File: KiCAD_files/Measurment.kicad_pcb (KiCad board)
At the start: 2 copper layers, 90 x 63 mm, 66 parts, among them J1 Board outline, J2 Measurment_stage_outline_sign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, J3 Conn_01x02, U1 NMA1505SC, U2 AMC1100, U3 AMC1100, U4 AMC1311, U5 R-78C5.0-1.0, U6 AMS1117-3.3, U7 NMA1505SC

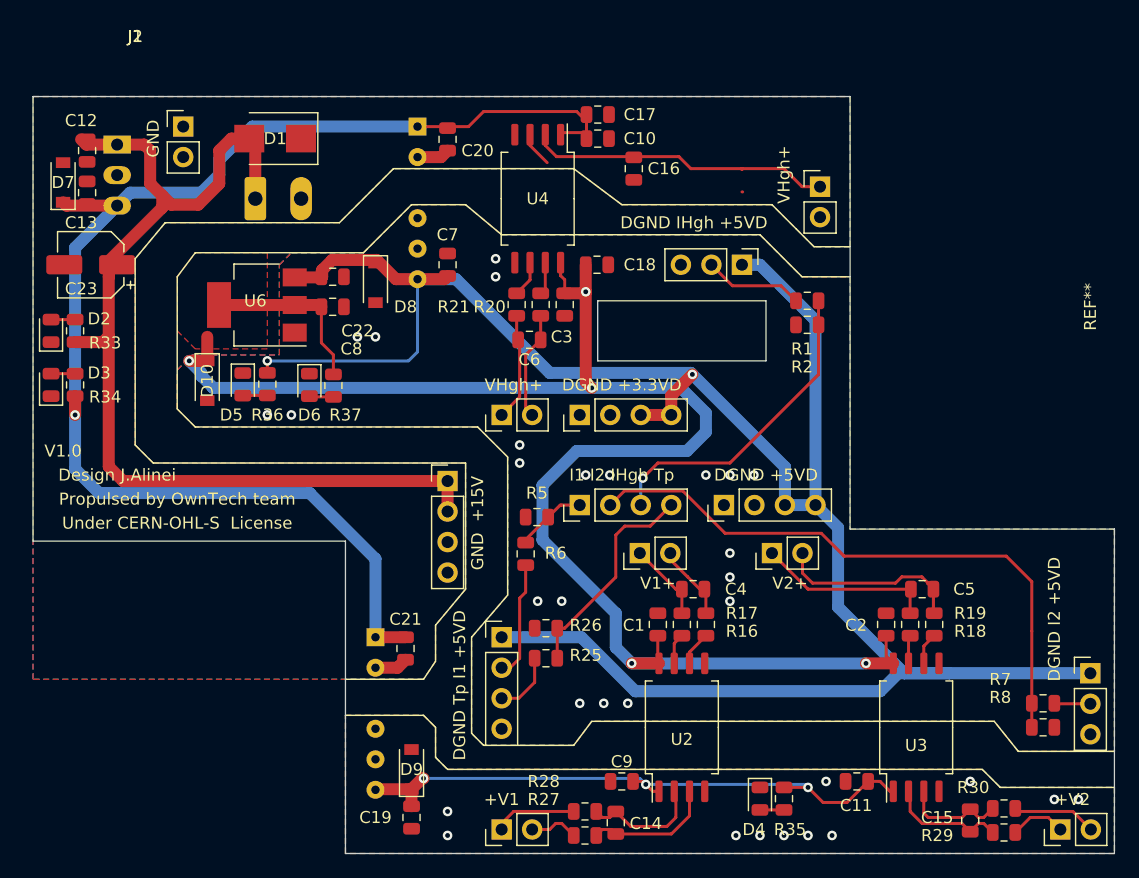
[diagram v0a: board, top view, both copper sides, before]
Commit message: Solved minor glitch on the overlay.
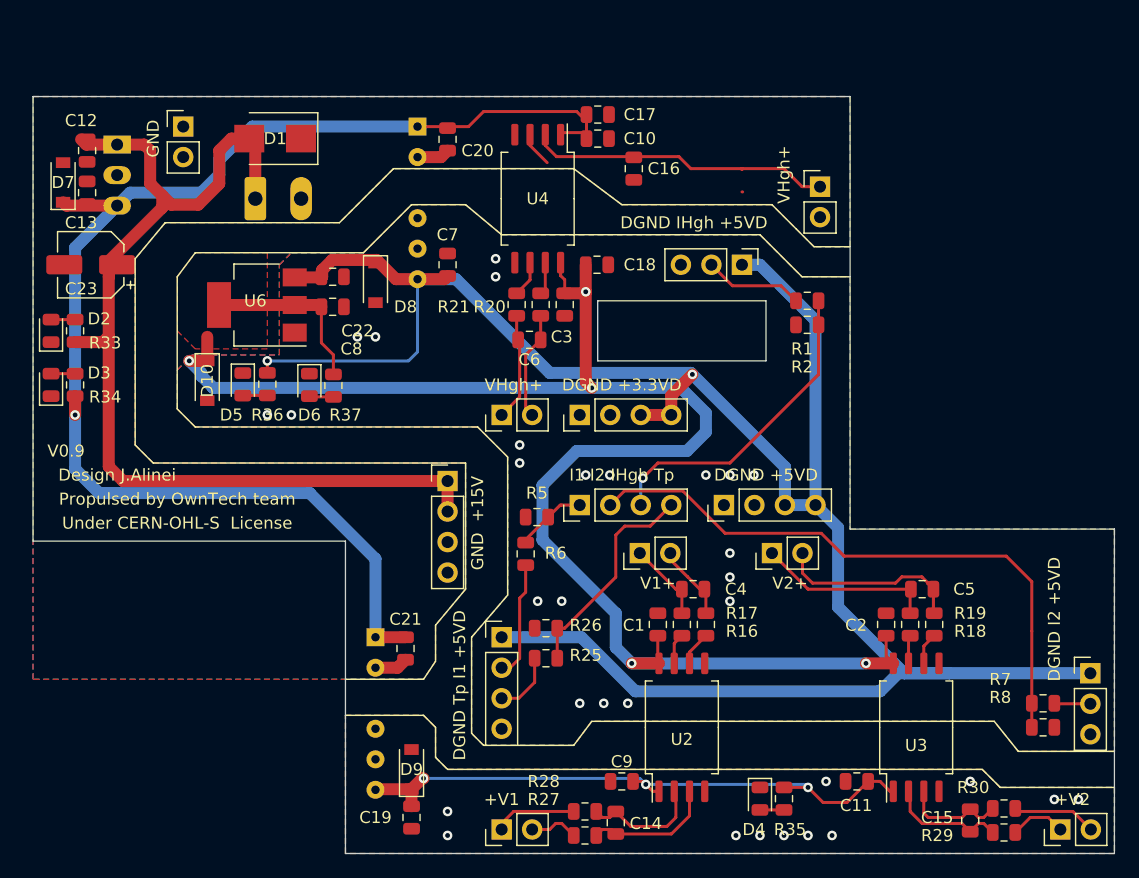
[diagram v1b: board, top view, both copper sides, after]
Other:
- board text added: "V0.9"
- board text removed: "V1.0"
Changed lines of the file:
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@@
   (general
     (thickness 1.6)
-    (drawings 66)
+    (drawings 64)
     (tracks 341)
     (zones 0)
@@
   (page A4)
   (layers
-    (0 F.Cu signal hide)
+    (0 F.Cu signal)
     (31 B.Cu signal hide)
     (32 B.Adhes user hide)
@@
   (module Footprints:Measurment_stage_outline_outputs (layer F.Cu)
     (at 31.5 41.5)
-    (fp_text reference J1 (at 8.5 -5 180) (layer F.SilkS)
+    (fp_text reference J1 (at 8.5 -5 180) (layer F.SilkS) hide
       (effects (font (size 1 1) (thickness 0.15)))
     )
@@
   (module Footprints:Measurment_stage_outline_inputs (layer F.Cu)
     (at 31.5 41.5)
-    (fp_text reference J2 (at 8.5 -5 180) (layer F.SilkS)
+    (fp_text reference J2 (at 8.5 -5 180) (layer F.SilkS) hide
       (effects (font (size 1 1) (thickness 0.15)))
     )
@@
     (fp_line (start 26 42) (end 26 63) (layer Eco2.User) (width 0.12))
     (fp_line (start 26 63) (end 90 63) (layer Eco2.User) (width 0.12))
-    (fp_text user REF** (at 88 17.5 270) (layer F.SilkS)
+    (fp_text user REF** (at 88 17.5 270) (layer F.SilkS) hide
       (effects (font (size 1 1) (thickness 0.15)))
     )
@@
       (effects (font (size 1 1) (thickness 0.15)) (justify mirror))
     )
-    (fp_text value Conn_01x02 (at 1.5 -18.5) (layer B.Fab)
+    (fp_text value Conn_01x02 (at 1.5 -18.5) (layer B.Fab) hide
       (effects (font (size 1 1) (thickness 0.15)) (justify mirror))
     )
@@
       (effects (font (size 1 1) (thickness 0.15)) (justify mirror))
     )
-    (fp_text value NMA1505SC (at 0.5 8.5 180) (layer B.Fab)
+    (fp_text value NMA1505SC (at 0.5 8.5 180) (layer B.Fab) hide
       (effects (font (size 1 1) (thickness 0.15)) (justify mirror))
     )
@@
       (effects (font (size 1 1) (thickness 0.15)) (justify mirror))
     )
-    (fp_text value NMA1505SC (at 9 -37) (layer B.Fab)
+    (fp_text value NMA1505SC (at 9 -37) (layer B.Fab) hide
       (effects (font (size 1 1) (thickness 0.15)) (justify mirror))
     )
@@
       (effects (font (size 1 1) (thickness 0.15)) (justify mirror))
     )
-    (fp_text value R-78C5.0-1.0 (at 3 16.5) (layer B.Fab)
+    (fp_text value R-78C5.0-1.0 (at 3 16.5) (layer B.Fab) hide
       (effects (font (size 1 1) (thickness 0.15)) (justify mirror))
     )
@@
     (effects (font (size 1 1) (thickness 0.15)))
   )
-  (gr_text "V1.0\n" (at 34 71) (layer F.SilkS)
+  (gr_text V0.9 (at 34.25 71) (layer F.SilkS)
     (effects (font (size 1 1) (thickness 0.15)))
   )
@@
   )
   (gr_line (start 31.5 41.5) (end 99.5 41.5) (layer Edge.Cuts) (width 0.05))
-  (gr_line (start 31.5 41.5) (end 26.5 41.5) (layer Dwgs.User) (width 0.15))
-  (gr_line (start 31.5 41.5) (end 31.5 38) (layer Dwgs.User) (width 0.15))
   (gr_line (start 80.5 50.5) (end 76.5 47.5) (layer F.SilkS) (width 0.12))
   (gr_line (start 93 50.5) (end 80.5 50.5) (layer F.SilkS) (width 0.12))

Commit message: Updated values in pcbnew - regenerated interactive BOM
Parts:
- C12, C20, C21: value C_Small -> 1uF
- C13, C19, C22, C7, C8: value C_Small -> 100nF
- D1: value D_TVS -> 1SMB5930BT3G
- J1: value Board outline -> Measurment_stage_outline_outputs
- R33: value R_Small -> 10k
- R34, R35, R36: value R_Small -> 2.2k
- R37: value R_Small -> 1k

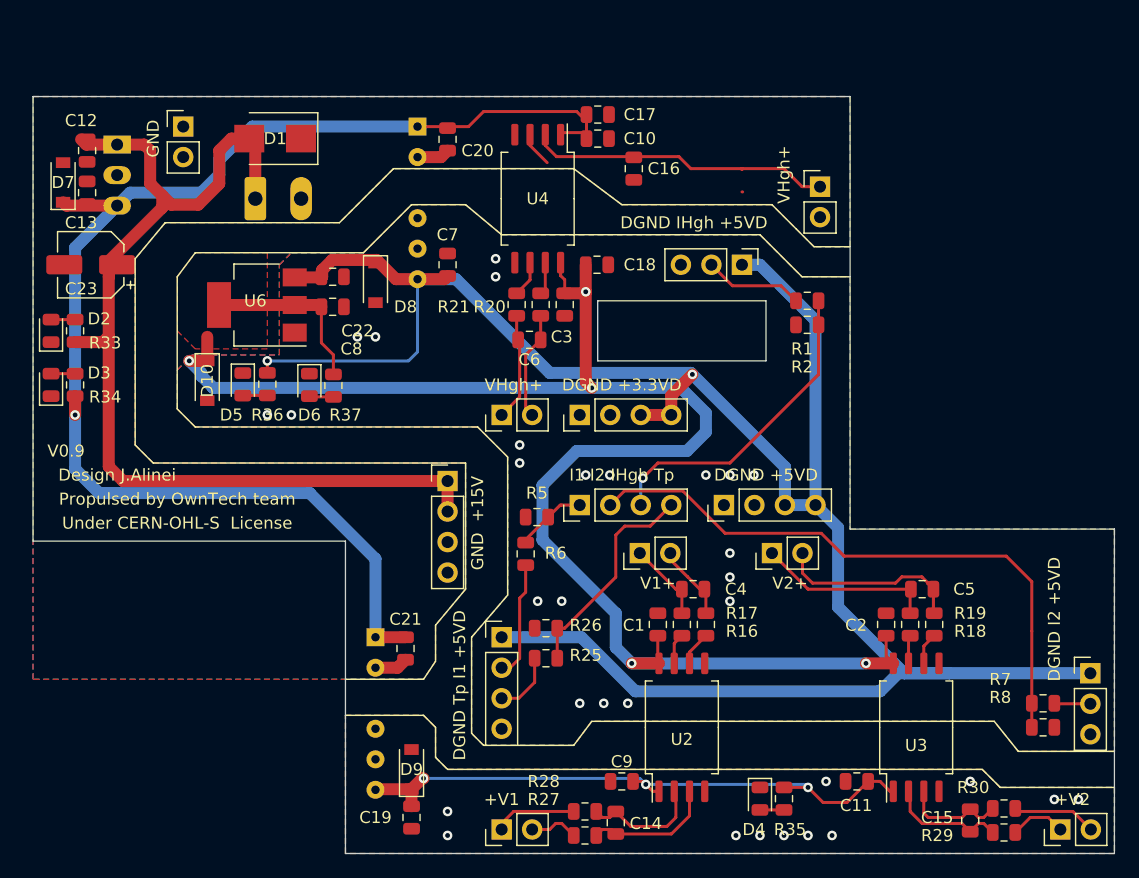
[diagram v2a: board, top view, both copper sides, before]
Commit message: Changed all the headers to improve mezzanine height
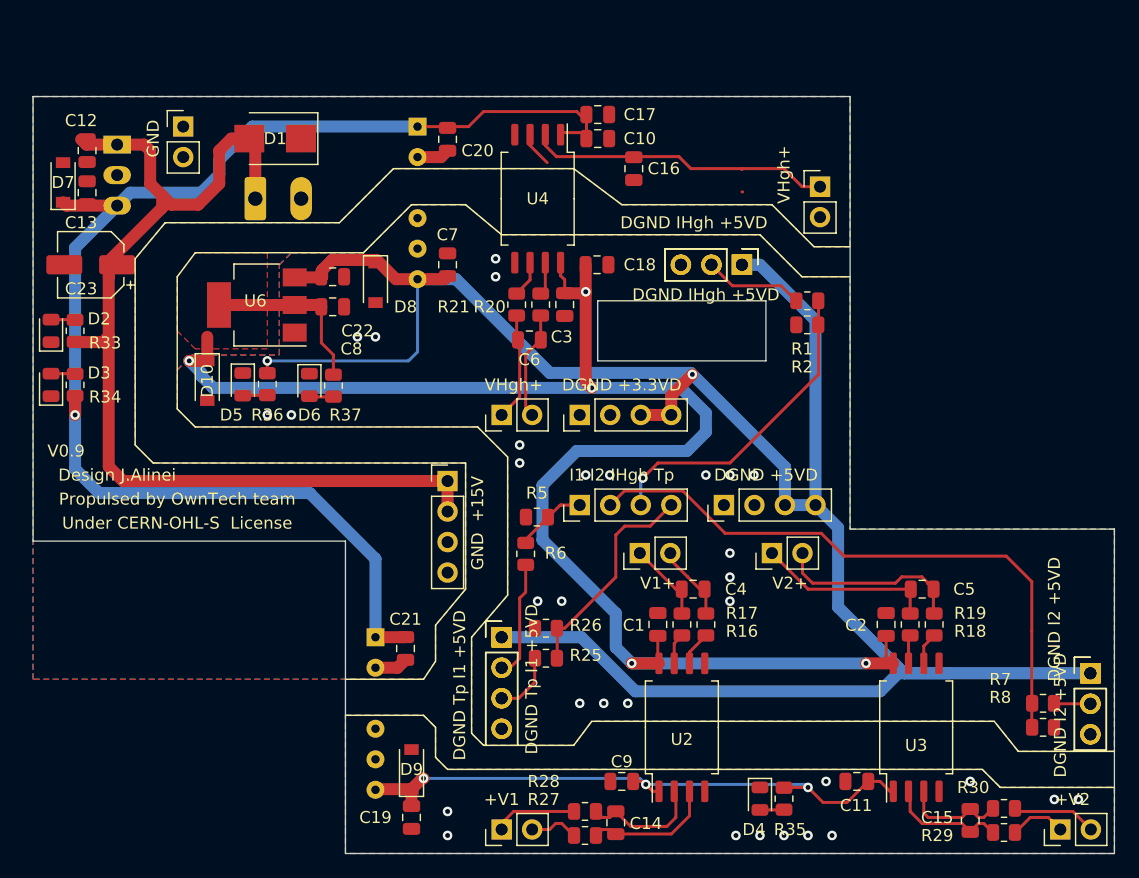
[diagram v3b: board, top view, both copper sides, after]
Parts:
- J1: value Measurment_stage_outline_outputs -> Board outline

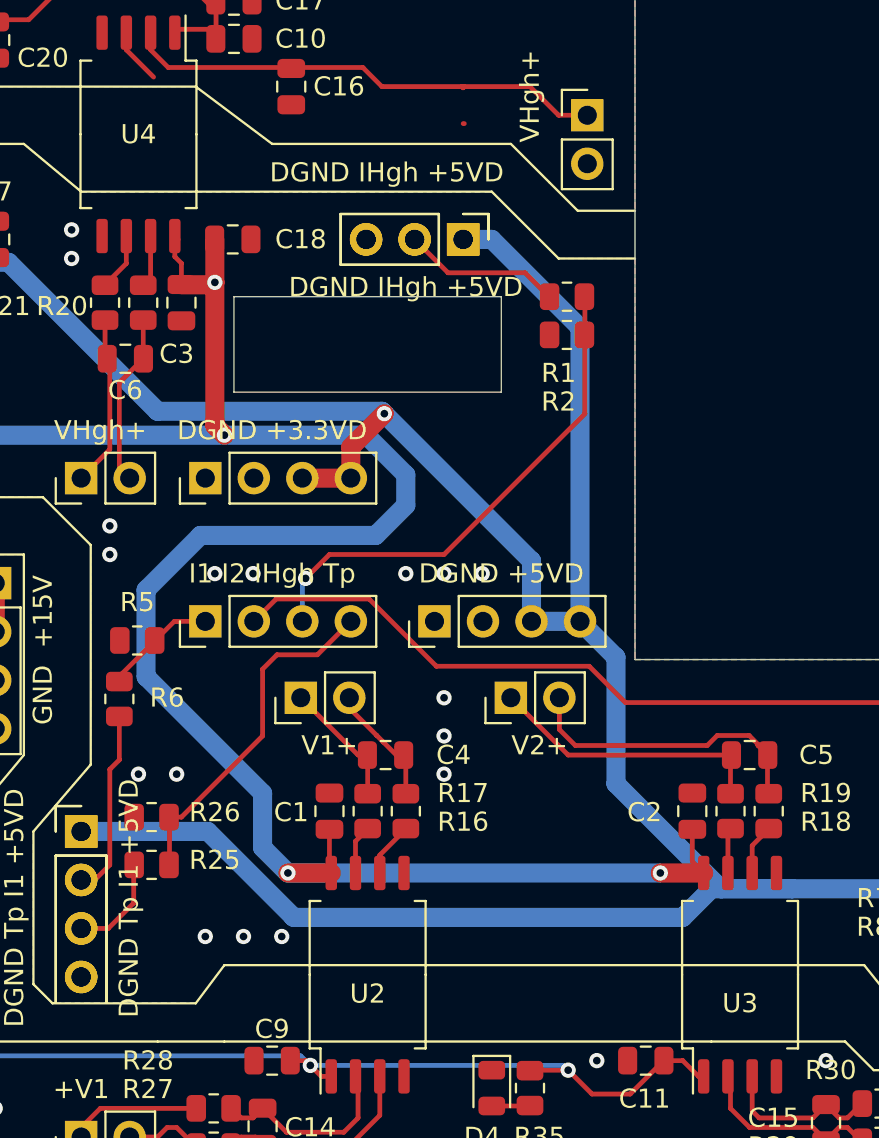
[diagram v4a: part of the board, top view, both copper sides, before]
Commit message: Added missing 3Dfootprints
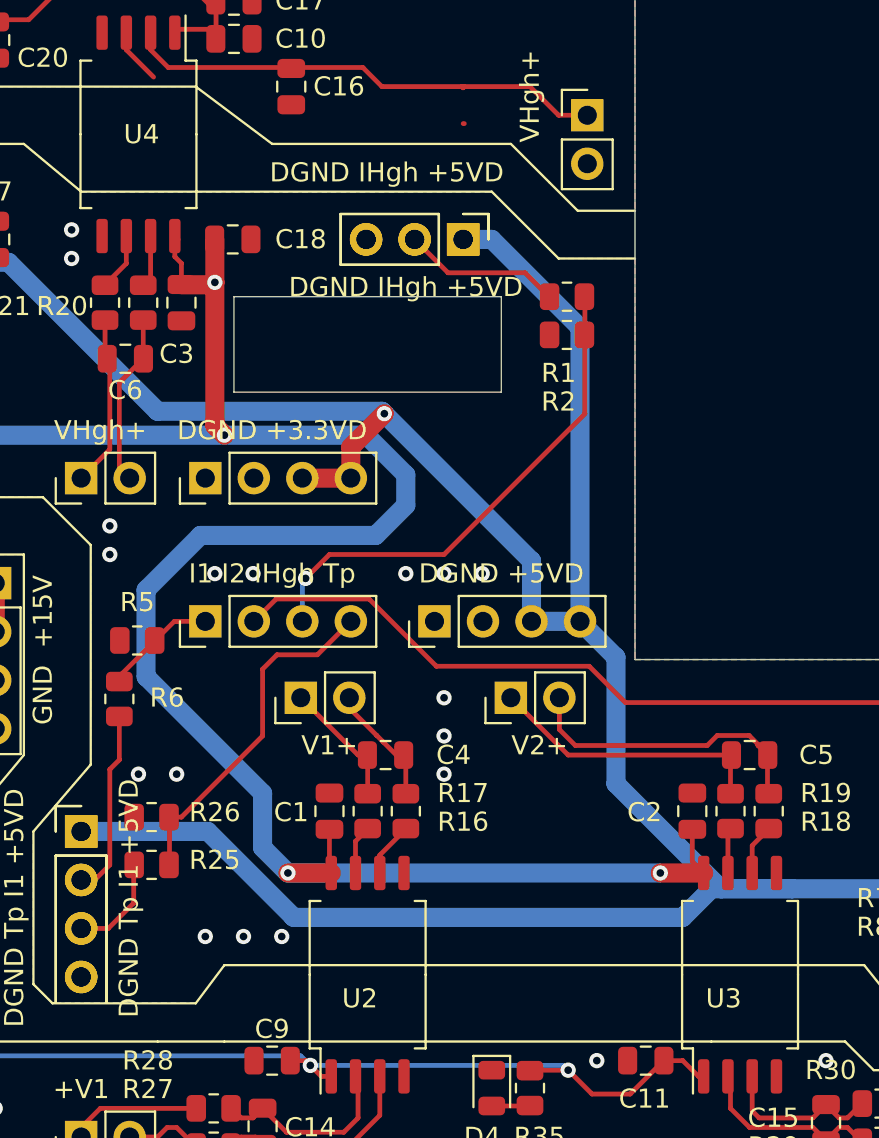
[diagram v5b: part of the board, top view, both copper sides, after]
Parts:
- J1: value Board outline -> Measurment_stage_outline_outputs
- U2, U3, U4: footprint Package_SO:SOIC-8_7.5x5.85mm_P1.27mm -> Footprints:SOIC-8_7.5x5.85mm_P1.27mm
